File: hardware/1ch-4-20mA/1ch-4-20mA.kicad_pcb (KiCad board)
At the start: 2 copper layers, 32.4 x 24.8 mm, 13 parts, among them J1 Conn_01x02, J2 Conn_01x03, U1 LMP8640

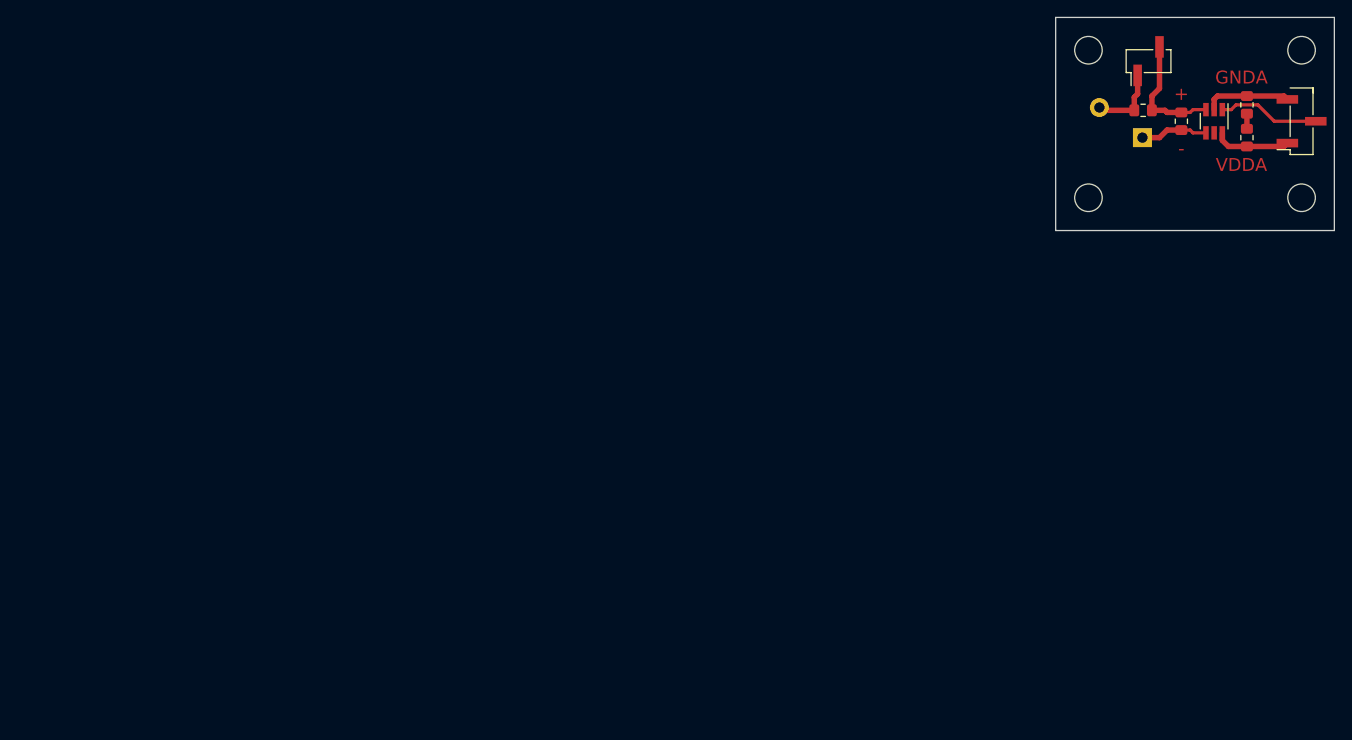
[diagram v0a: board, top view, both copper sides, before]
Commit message: Small info changes
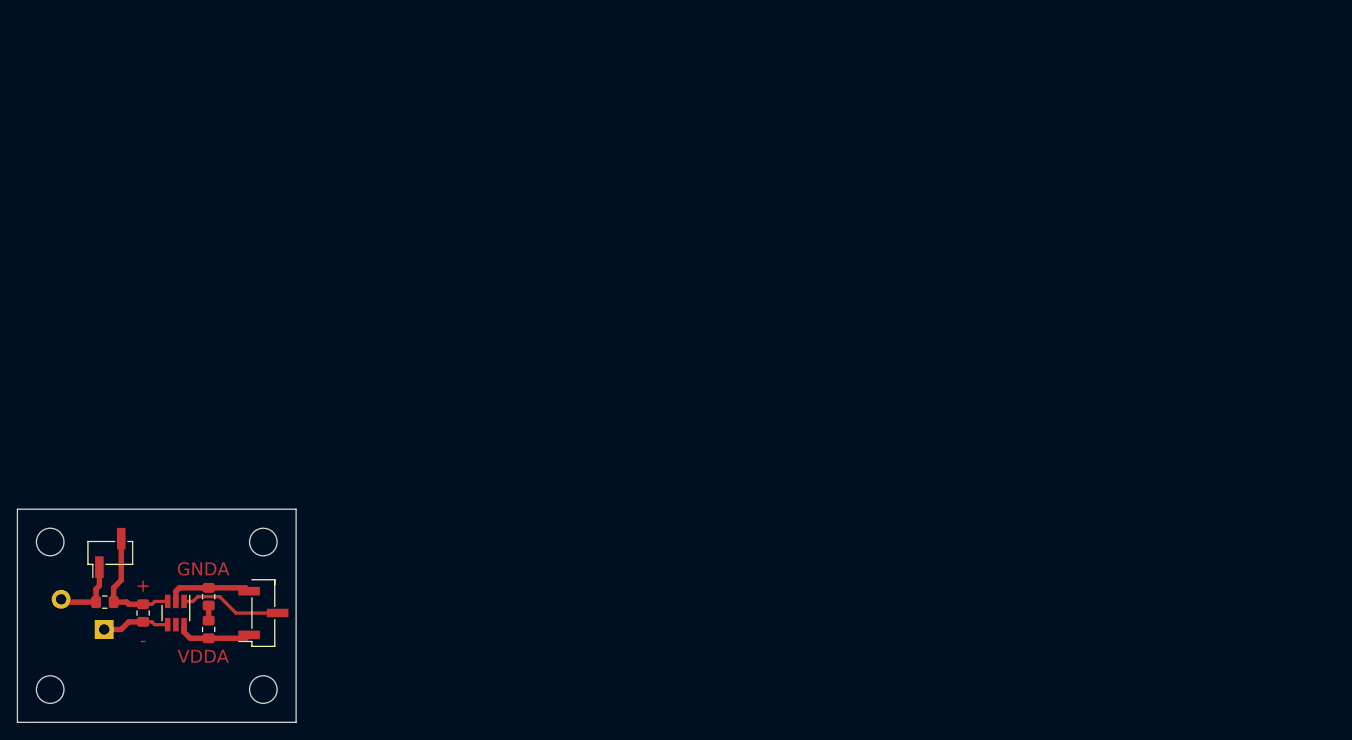
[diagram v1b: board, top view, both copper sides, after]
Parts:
- moved C1 133.5 mm to (151.8, 86.4)
- moved R1 133.5 mm to (139.7, 83.2)
- moved R3 133.5 mm to (151.8, 82.5)
- moved G1 133.5 mm to (145.4, 92.7)
- moved H1 133.5 mm to (133.3, 76.2)
- moved H4 133.5 mm to (133.3, 93.3)
- moved J1 133.5 mm to (134.6, 86.4)
- moved JP1 133.5 mm to (140.3, 77.5)
- moved R2 133.5 mm to (144.1, 84.5)
- moved U1 133.5 mm to (148.0, 84.5)
- moved H2 133.5 mm to (158.1, 76.2)
- moved H3 133.5 mm to (158.1, 93.3)
- moved J2 133.5 mm to (158.1, 84.5)
